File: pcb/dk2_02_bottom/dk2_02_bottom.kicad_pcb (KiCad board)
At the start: 2 copper layers, 140 x 108 mm, 174 parts, among them J1 Micro_SD_Card, J10 Trigger_Out_1, J11 Trigger_Out_4, J12 Trigger_Out_3, J13 Sync_Out, J14 Eurorack_Power, J2 CV_In_1, J3 CV_In_2, J4 CV_In_3, J5 CV_In_4, J6 Euro_Out_1, J7 Euro_Out_2, J8 Sync_Input, J9 Trigger_Out_2, Q1 MMBT3904, SW1 SW_Push, SW10 SW_Push, SW11 SW_Push, SW12 SW_Push, SW13 SW_Push, SW14 SW_Push, SW15 SW_Push, SW16 SW_Push, SW17 SW_Push, SW18 SW_Push, SW2 SW_Push, SW3 SW_Push, SW4 SW_Push, SW5 SW_Push, SW6 SW_Push, SW7 SW_Push, SW8 SW_Push, SW9 SW_Push, U1 Pico, U10 74HC4051, U11 AP7333-33SRG, U12 TL072, U13 PCM5102, U14 TL072, U15 TL072, U16 TL072, U17 XL1509-5.0, U2 74HC595, U3 74HC595, U4 CA56-12EWA, U5 74HC165, U6 74HC165, U7 74HC4051, U8 MCP6002-xSN, U9 MCP6002-xSN

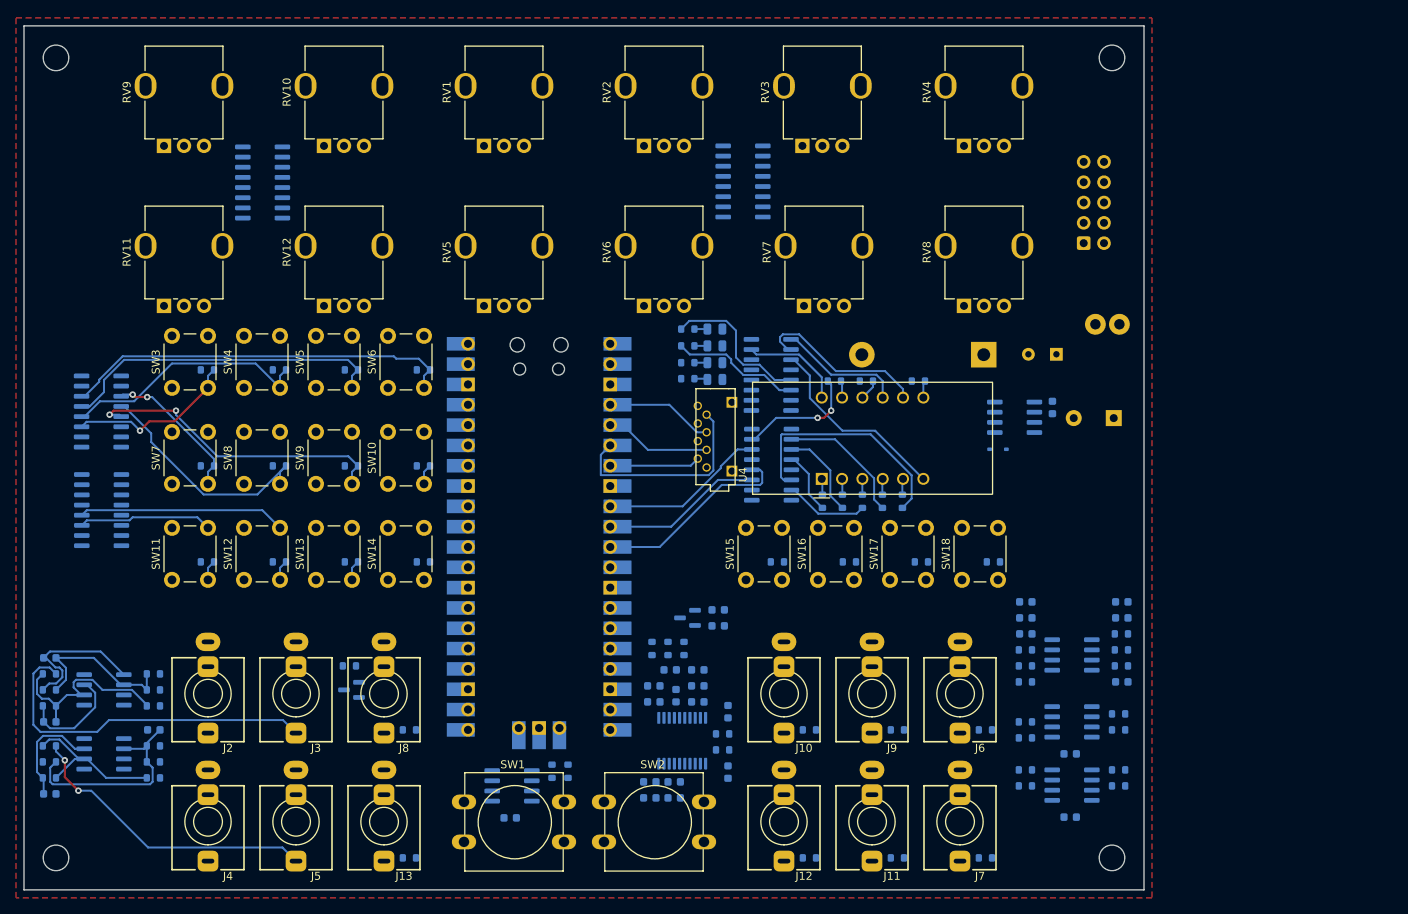
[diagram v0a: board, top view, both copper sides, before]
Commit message: bottom pcb looks fairly easy
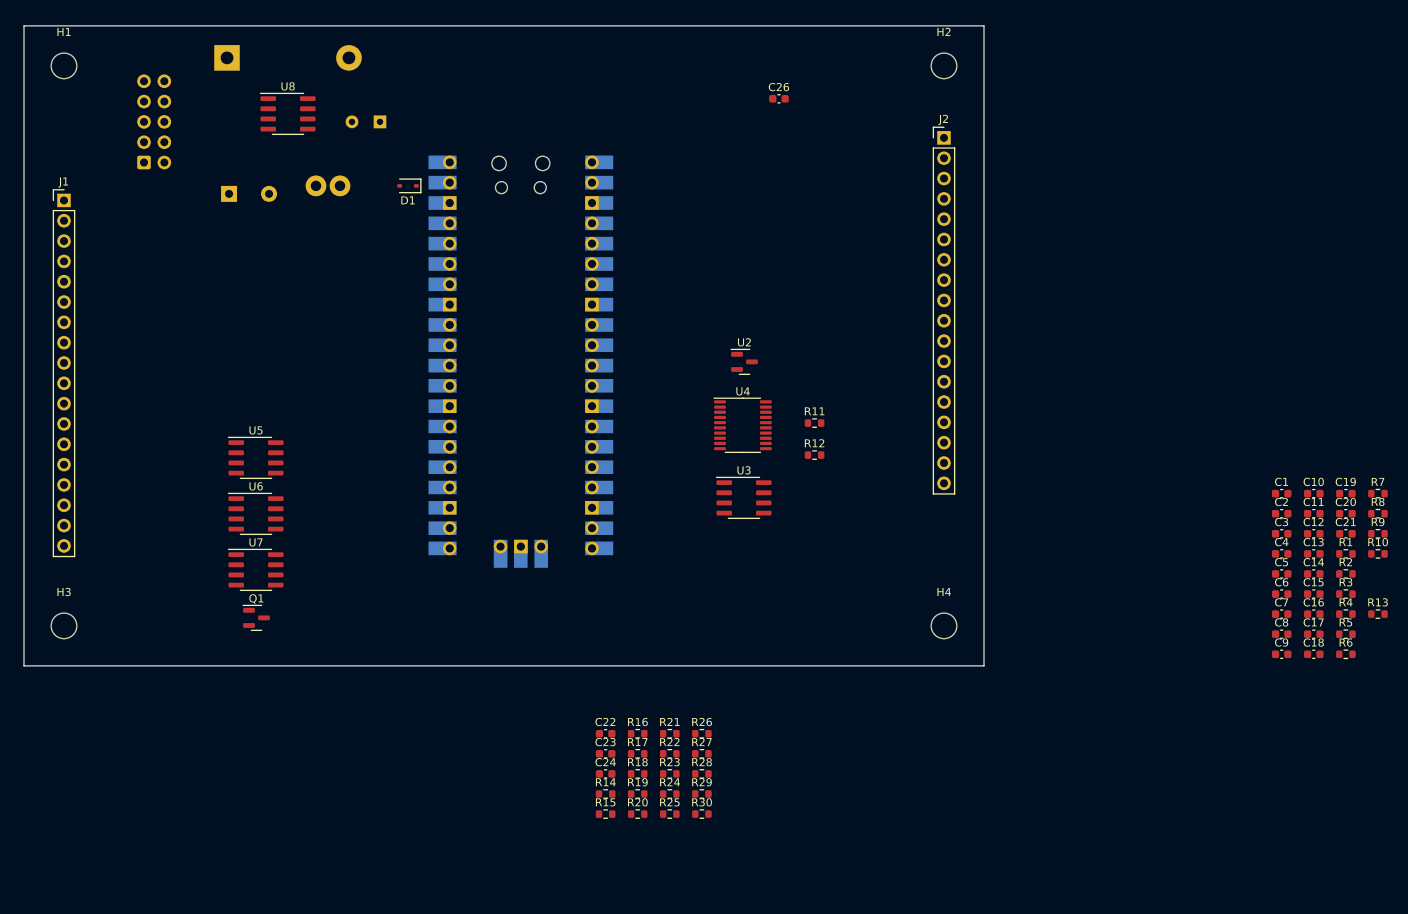
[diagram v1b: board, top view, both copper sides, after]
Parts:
- removed C28: 100n, Capacitor_SMD:C_0603_1608Metric
- removed C29: 470uF 35V, Capacitor_THT:CP_Radial_D10.0mm_P5.00mm
- removed C30: 1uF, Capacitor_SMD:C_0603_1608Metric
- removed C31: 180uF 35V, Capacitor_THT:CP_Radial_D8.0mm_P3.50mm
- removed D3, D4, D5: LED, LED_SMD:LED_0805_2012Metric
- removed D6: 1N5820, Diode_THT:D_DO-201AD_P15.24mm_Horizontal
- removed J10: Trigger_Out_1, AudioJacks:Jack_3.5mm_QingPu_WQP-PJ398SM_Vertical
- removed J11: Trigger_Out_4, AudioJacks:Jack_3.5mm_QingPu_WQP-PJ398SM_Vertical
- removed J12: Trigger_Out_3, AudioJacks:Jack_3.5mm_QingPu_WQP-PJ398SM_Vertical
- removed J13: Sync_Out, AudioJacks:Jack_3.5mm_QingPu_WQP-PJ398SM_Vertical
- removed J14: Eurorack_Power, Connector_IDC:IDC-Header_2x05_P2.54mm_Vertical
- removed J4: CV_In_3, AudioJacks:Jack_3.5mm_QingPu_WQP-PJ398SM_Vertical
- removed J5: CV_In_4, AudioJacks:Jack_3.5mm_QingPu_WQP-PJ398SM_Vertical
- removed J6: Euro_Out_1, AudioJacks:Jack_3.5mm_QingPu_WQP-PJ398SM_Vertical
- removed J7: Euro_Out_2, AudioJacks:Jack_3.5mm_QingPu_WQP-PJ398SM_Vertical
- removed J8: Sync_Input, AudioJacks:Jack_3.5mm_QingPu_WQP-PJ398SM_Vertical
- removed J9: Trigger_Out_2, AudioJacks:Jack_3.5mm_QingPu_WQP-PJ398SM_Vertical
- removed R31, R35, R37: 240k, Resistor_SMD:R_0603_1608Metric
- removed R32, R36, R38, R56, R57, R58, R59, R62, R63, R64, R65, R68, R69: 100k, Resistor_SMD:R_0603_1608Metric
- removed R33, R34, R39, R40: 33k, Resistor_SMD:R_0603_1608Metric
- removed R41, R42, R45, R46: 39k, Resistor_SMD:R_0603_1608Metric
- removed R43, R44: 5.6k, Resistor_SMD:R_0603_1608Metric
- removed R47, R48, R60, R61, R66, R67, R70: 1k, Resistor_SMD:R_0603_1608Metric
- removed R49, R50, R51: 56R, Resistor_SMD:R_0603_1608Metric
- removed R52, R53: 470R, Resistor_SMD:R_0603_1608Metric
- removed R54: 100K, Resistor_SMD:R_0603_1608Metric
- removed R55: 10K, Resistor_SMD:R_0603_1608Metric
- removed RV1, RV10, RV11, RV12, RV2, RV3, RV4, RV5, RV6, RV7, RV8, RV9: 10k, Library:Potentiometer_Alps_RK09K_vertical_biggerholes
- removed SW1, SW2: SW_Push, Button_Switch_THT:SW_PUSH-12mm
- removed SW10, SW11, SW12, SW13, SW14, SW15, SW16, SW17, SW18, SW3, SW4, SW5, SW6, SW7, SW8, SW9: SW_Push, Button_Switch_THT:SW_PUSH_6mm
- removed U10: 74HC4051, Package_SO:SOIC-16_3.9x9.9mm_P1.27mm
- removed U11: AP7333-33SRG, Package_TO_SOT_SMD:SOT-23
- removed U12, U14, U15, U16: TL072, Package_SO:SOIC-8_3.9x4.9mm_P1.27mm
- removed U13: PCM5102, Package_SO:TSSOP-20_4.4x6.5mm_P0.65mm
- removed U17: XL1509-5.0, Package_SO:SOIC-8_3.9x4.9mm_P1.27mm
- removed U9: MCP6002-xSN, Package_SO:SOIC-8_3.9x4.9mm_P1.27mm
- C1, C4: value 1n -> 1uF; moved to F.Cu
- C10, C26: value 100n -> 1uF; moved to F.Cu
- C11: value 18p -> 10uF; moved to F.Cu
- C12: value 18p -> 2.2uF; moved to F.Cu
- C13: value 0.1uF -> 2.2uF; moved to F.Cu
- C14: value 1uF -> 0.1uF; moved to F.Cu
- C15: value 10uF -> 1uF; moved to F.Cu
- C16: value 2.2uF -> 10uF; moved to F.Cu
- C17: value 2.2uF -> 0.1uF; moved to F.Cu
- C18, C20, D1, Q1: moved to F.Cu
- C19: value 1uF -> 2.2nF; moved to F.Cu
- C2, C3: value 1n -> 10uF; moved to F.Cu
- C21: value 0.1uF -> 2.2nF; moved to F.Cu
- C22: value 0.1uF -> 100n; moved to F.Cu
- C23: value 2.2nF -> 100n; moved to F.Cu
- C24, C6: value 10uF -> 100n; moved to F.Cu
- C25: value 2.2nF -> 470uF 35V; footprint Capacitor_SMD:C_0603_1608Metric -> Capacitor_THT:CP_Radial_D10.0mm_P5.00mm
- C27: value 100n -> 180uF 35V; footprint Capacitor_SMD:C_0603_1608Metric -> Capacitor_THT:CP_Radial_D8.0mm_P3.50mm
- C5: value 1uF -> 100n; moved to F.Cu
- C7: value 10uF -> 18p; moved to F.Cu
- C8: value 1uF -> 18p; moved to F.Cu
- C9: value 100n -> 0.1uF; moved to F.Cu
- D2: value LED -> 1N5820; footprint LED_SMD:LED_0805_2012Metric -> Diode_THT:D_DO-201AD_P15.24mm_Horizontal
- J1: value Micro_SD_Card -> Conn_01x18_Pin; footprint misc:YAMAICHI_MICROSD_VERTICAL -> Connector_PinHeader_2.54mm:PinHeader_1x18_P2.54mm_Vertical
- J2: value CV_In_1 -> Conn_01x18_Pin; footprint AudioJacks:Jack_3.5mm_QingPu_WQP-PJ398SM_Vertical -> Connector_PinHeader_2.54mm:PinHeader_1x18_P2.54mm_Vertical
- J3: value CV_In_2 -> Eurorack_Power; footprint AudioJacks:Jack_3.5mm_QingPu_WQP-PJ398SM_Vertical -> Connector_IDC:IDC-Header_2x05_P2.54mm_Vertical; moved to B.Cu
- R1, R2, R5, R6: value 200R -> 39k; moved to F.Cu
- R10, R11, R9: value 200R -> 56R; moved to F.Cu
- R12: value 200R -> 470R; moved to F.Cu
- R13: value 10k -> 470R; moved to F.Cu
- R14: value 10k -> 100K; moved to F.Cu
- R15: value 10k -> 10K; moved to F.Cu
- R16, R17, R18, R19, R22, R23, R24, R25, R28: value 10k -> 100k; moved to F.Cu
- R20, R21, R26, R27: value 10k -> 1k; moved to F.Cu
- R29: value 240k -> 100k; moved to F.Cu
- R3, R4: value 200R -> 5.6k; moved to F.Cu
- R30: value 100k -> 1k; moved to F.Cu
- R7, R8: value 200R -> 1k; moved to F.Cu
- U2: value 74HC595 -> AP7333-33SRG; footprint Package_SO:SOIC-16_3.9x9.9mm_P1.27mm -> Package_TO_SOT_SMD:SOT-23; moved to F.Cu
- U3: value 74HC595 -> TL072; footprint Package_SO:SOIC-16_3.9x9.9mm_P1.27mm -> Package_SO:SOIC-8_3.9x4.9mm_P1.27mm; moved to F.Cu
- U4: value CA56-12EWA -> PCM5102; footprint Library:SR410361N -> Package_SO:TSSOP-20_4.4x6.5mm_P0.65mm
- U5, U6: value 74HC165 -> TL072; footprint Package_SO:SOIC-16_3.9x9.9mm_P1.27mm -> Package_SO:SOIC-8_3.9x4.9mm_P1.27mm; moved to F.Cu
- U7: value 74HC4051 -> TL072; footprint Package_SO:SOIC-16_3.9x9.9mm_P1.27mm -> Package_SO:SOIC-8_3.9x4.9mm_P1.27mm; moved to F.Cu
- U8: value MCP6002-xSN -> XL1509-5.0; moved to F.Cu
- moved C4 156.9 mm to (237.2, 116.0), turned to 0 degrees
- moved C2 156.2 mm to (237.2, 111.0), turned to 0 degrees
- moved C1 155.4 mm to (237.2, 108.5), turned to 0 degrees
- moved R13 149.5 mm to (249.2, 123.5), turned to 0 degrees
- moved C3 143.1 mm to (237.2, 113.5), turned to 0 degrees
- moved C27 117.0 mm to (124.5, 62.0), turned to 180 degrees
- moved J2 115.3 mm to (195.0, 64.0), turned to 0 degrees
- moved L1 101.9 mm to (116.5, 70.0), turned to 0 degrees
- moved C26 96.9 mm to (174.4, 59.1)
- moved C25 95.5 mm to (105.6, 71.0), turned to 0 degrees
- moved C20 94.0 mm to (245.2, 111.0), turned to 0 degrees
- moved C19 91.4 mm to (245.2, 108.5)
- moved C21 90.2 mm to (245.2, 113.5)
- moved R4 88.1 mm to (245.2, 123.5), turned to 0 degrees
- moved R3 87.9 mm to (245.2, 121.0), turned to 0 degrees
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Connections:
- C1 pad 1: Net-(U8A--) -> +5V
- C1 pad 2: CV_IN_1 -> GND
- C10 pad 1: GND -> +3.3VDAC
- C10 pad 2: -12V -> GND
- C11 pad 1: Net-(U12A--) -> +3.3VDAC
- C11 pad 2: Net-(C11-Pad2) -> GND
- C12 pad 1: Net-(U12B--) -> Net-(U4-CAPP)
- C12 pad 2: Net-(C12-Pad2) -> Net-(U4-CAPM)
- C13 pad 1: +3.3VDAC -> Net-(U4-VNEG)
- C15 pad 1: +3.3VDAC -> Net-(U4-LDOO)
- C16 pad 1: Net-(U13-CAPP) -> +3.3VDAC
- C16 pad 2: Net-(U13-CAPM) -> GND
- C17 pad 1: Net-(U13-VNEG) -> Net-(U4-LDOO)
- C19 pad 1: Net-(U13-LDOO) -> LINE_OUT_L
- C2 pad 1: Net-(U8B--) -> LINE_OUT_L
- C2 pad 2: CV_IN_2 -> Net-(C2-Pad2)
- C21 pad 1: Net-(U13-LDOO) -> LINE_OUT_R
- C22 pad 1: +3.3VDAC -> +12V
- C22 pad 2: GND -> -12V
- C23 pad 1: LINE_OUT_L -> +12V
- C23 pad 2: GND -> -12V
- C24 pad 1: +3.3VDAC -> +12V
- C24 pad 2: GND -> -12V
- C25 pad 1: LINE_OUT_R -> +12V
- C26 pad 2: -12V -> GND
- C27 pad 1: +12V -> +5V
- C27 pad 2: -12V -> GND
- C3 pad 1: Net-(U9A--) -> LINE_OUT_R
- C3 pad 2: CV_IN_3 -> Net-(C3-Pad2)
- C4 pad 1: Net-(U9B--) -> +3.3VDAC
- C4 pad 2: CV_IN_4 -> GND
- C5 pad 1: +5V -> +12V
- C6 pad 1: LINE_OUT_L -> GND
- C6 pad 2: Net-(C6-Pad2) -> -12V
- C7 pad 1: LINE_OUT_R -> Net-(U3A--)
- C8 pad 1: +3.3VDAC -> Net-(U3B--)
- C8 pad 2: GND -> Net-(C8-Pad2)
- C9 pad 1: +12V -> +3.3VDAC
- D2 pad 1: GND -> Net-(D2-K)
- D2 pad 2: Net-(D2-A) -> GND
- J1 pad 2: SD_CHIP_SELECT -> unconnected-(J1-Pin_2-Pad2)
- J1 pad 3: SD_SERIAL_IN -> unconnected-(J1-Pin_3-Pad3)
- J1 pad 4: +3.3V -> START_STOP_BUTTON
- J1 pad 5: SD_CLOCK -> TAP_TEMPO_BUTTON
- J1 pad 6: GND -> 165_LOAD
- J1 pad 7: SD_SERIAL_OUT -> 165_CLOCK
- J1 pad 8: unconnected-(J1-DAT1-Pad8) -> 165_DATA
- J1 pad 9: GND -> TRIGGER_OUT_1_EURO
- L1 pad 1: Net-(D6-K) -> Net-(D2-K)
- R1 pad 1: Net-(D2-A) -> Net-(C2-Pad2)
- R1 pad 2: Net-(U3-QE) -> GND
- R10 pad 1: Net-(U4-f) -> DAC_DOUT
- R10 pad 2: Net-(U2-QF) -> Net-(U4-DIN)
- R11 pad 1: Net-(U4-g) -> DAC_LRC
- R11 pad 2: Net-(U2-QG) -> Net-(U4-LRCK)
- R12 pad 1: Net-(U4-DPX) -> Net-(U4-OUTL)
- R12 pad 2: Net-(U2-QH) -> LINE_OUT_L
- R13 pad 1: Net-(U5-D0) -> Net-(U4-OUTR)
- R13 pad 2: GND -> LINE_OUT_R
- R14 pad 1: Net-(U5-D1) -> SYNC_IN_EURO
- R14 pad 2: GND -> Net-(Q1-B)
- R15 pad 1: Net-(U5-D2) -> +3.3V
- R15 pad 2: GND -> SYNC_IN
- R16 pad 1: Net-(U5-D3) -> Net-(U5B--)
- R17 pad 1: Net-(U5-D4) -> Net-(U5A--)
- R18 pad 1: Net-(U5-D5) -> Net-(R18-Pad1)
- R18 pad 2: GND -> Net-(U5B--)
- R19 pad 1: Net-(U5-D6) -> Net-(R19-Pad1)
- R19 pad 2: GND -> Net-(U5A--)
- R2 pad 1: Net-(D3-A) -> Net-(C3-Pad2)
- R2 pad 2: Net-(U3-QF) -> GND
- R20 pad 1: Net-(U5-D7) -> Net-(R18-Pad1)
- R20 pad 2: GND -> TRIGGER_OUT_2_EURO
- R21 pad 1: Net-(U6-D0) -> Net-(R19-Pad1)
- R21 pad 2: GND -> TRIGGER_OUT_1_EURO
- R22 pad 1: Net-(U6-D1) -> Net-(U6B--)
- R23 pad 1: Net-(U6-D2) -> Net-(U6A--)
- R24 pad 1: Net-(U6-D3) -> Net-(R24-Pad1)
- R24 pad 2: GND -> Net-(U6B--)
- R25 pad 1: Net-(U6-D4) -> Net-(R25-Pad1)
- R25 pad 2: GND -> Net-(U6A--)
- R26 pad 1: Net-(U6-D5) -> Net-(R24-Pad1)
- R26 pad 2: GND -> TRIGGER_OUT_4_EURO
- R27 pad 1: Net-(U6-D6) -> Net-(R25-Pad1)
- R27 pad 2: GND -> TRIGGER_OUT_3_EURO
- R28 pad 1: Net-(U6-D7) -> Net-(U7A--)
- R29 pad 1: -12V -> Net-(R29-Pad1)
- R29 pad 2: Net-(U8A--) -> Net-(U7A--)
- R3 pad 1: Net-(D4-A) -> Net-(C2-Pad2)
- R3 pad 2: Net-(U3-QG) -> Net-(U3A--)
- R30 pad 1: Net-(J2-PadT) -> Net-(R29-Pad1)
- R30 pad 2: Net-(U8A--) -> SYNC_OUT_EURO
- R4 pad 1: Net-(D5-A) -> Net-(C3-Pad2)
- R4 pad 2: Net-(U3-QH) -> Net-(U3B--)
- R5 pad 1: Net-(U4-a) -> Net-(U3A--)
- R5 pad 2: Net-(U2-QA) -> Net-(C7-Pad2)
- R6 pad 1: Net-(U4-b) -> Net-(U3B--)
- R6 pad 2: Net-(U2-QB) -> Net-(C8-Pad2)
- R7 pad 1: Net-(U4-c) -> Net-(C7-Pad2)
- R7 pad 2: Net-(U2-QC) -> EURO_OUT_1
- R8 pad 1: Net-(U4-d) -> Net-(C8-Pad2)
- R8 pad 2: Net-(U2-QD) -> EURO_OUT_2
- R9 pad 1: Net-(U4-e) -> DAC_BCLK
- R9 pad 2: Net-(U2-QE) -> Net-(U4-BCK)
- U2 pad 1: Net-(U2-QB) -> +5V
- U2 pad 2: Net-(U2-QC) -> +3.3VDAC
- U2 pad 3: Net-(U2-QD) -> GND
- U3 pad 1: Net-(U3-QB) -> Net-(C7-Pad2)
- U3 pad 2: Net-(U3-QC) -> Net-(U3A--)
- U3 pad 3: Net-(U3-QD) -> GND
- U3 pad 4: Net-(U3-QE) -> -12V
- U3 pad 5: Net-(U3-QF) -> GND
- U3 pad 6: Net-(U3-QG) -> Net-(U3B--)
- U3 pad 7: Net-(U3-QH) -> Net-(C8-Pad2)
- U3 pad 8: GND -> +12V
- U4 pad 1: Net-(U4-e) -> +3.3VDAC
- U4 pad 10: Net-(U4-f) -> GND
- U4 pad 11: Net-(U4-a) -> GND
- U4 pad 12: Net-(U3-QA) -> GND
- U4 pad 2: Net-(U4-d) -> Net-(U4-CAPP)
- U4 pad 3: Net-(U4-DPX) -> GND
- U4 pad 4: Net-(U4-c) -> Net-(U4-CAPM)
- U4 pad 5: Net-(U4-g) -> Net-(U4-VNEG)
- U4 pad 6: Net-(U3-QD) -> Net-(U4-OUTL)
- U4 pad 7: Net-(U4-b) -> Net-(U4-OUTR)
- U4 pad 8: Net-(U3-QC) -> +3.3VDAC
- U4 pad 9: Net-(U3-QB) -> GND
- U5 pad 1: 165_LOAD -> Net-(R19-Pad1)
- U5 pad 2: 165_CLOCK -> Net-(U5A--)
- U5 pad 3: Net-(U5-D4) -> TRIGGER_OUT_1
- U5 pad 4: Net-(U5-D5) -> -12V
- U5 pad 5: Net-(U5-D6) -> TRIGGER_OUT_2
- U5 pad 6: Net-(U5-D7) -> Net-(U5B--)
- U5 pad 7: unconnected-(U5-~{Q7}-Pad7) -> Net-(R18-Pad1)
- U5 pad 8: GND -> +12V
- U6 pad 1: 165_LOAD -> Net-(R25-Pad1)
- U6 pad 2: 165_CLOCK -> Net-(U6A--)
- U6 pad 3: Net-(U6-D4) -> TRIGGER_OUT_3
- U6 pad 4: Net-(U6-D5) -> -12V
- U6 pad 5: Net-(U6-D6) -> TRIGGER_OUT_4
- U6 pad 6: Net-(U6-D7) -> Net-(U6B--)
- U6 pad 7: unconnected-(U6-~{Q7}-Pad7) -> Net-(R24-Pad1)
- U6 pad 8: GND -> +12V
- U7 pad 1: Net-(U7-A4) -> Net-(R29-Pad1)
- U7 pad 2: Net-(U7-A6) -> Net-(U7A--)
- U7 pad 3: 4051_READING_0 -> SYNC_OUT
- U7 pad 4: Net-(U7-A7) -> -12V
- U7 pad 5: Net-(U7-A5) -> GND
- U7 pad 6: GND -> Net-(U7B--)
- U7 pad 7: GND -> Net-(U7B--)
- U7 pad 8: GND -> +12V
- U8 pad 1: CV_IN_1 -> +12V
- U8 pad 2: Net-(U8A--) -> Net-(D2-K)
- U8 pad 3: GND -> +5V
- U8 pad 6: Net-(U8B--) -> GND
- U8 pad 7: CV_IN_2 -> GND
- U8 pad 8: +3.3V -> GND
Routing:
- net Net-(U5-D3): track 49.0 -> 0.00 mm
- net Net-(J3-PadT): track 44.4 -> 0.00 mm
- net Net-(U5-D2): track 40.9 -> 0.00 mm
- net Net-(U5-D6): track 38.5 -> 0.00 mm, vias 2 -> 0
- net Net-(J5-PadT): track 37.6 -> 0.00 mm, vias 2 -> 0
- net Net-(U5-D1): track 31.4 -> 0.00 mm
- net Net-(U5-D5): track 29.8 -> 0.00 mm
- net Net-(U2-QG): track 29.7 -> 0.00 mm
- net Net-(U6-D1): track 28.5 -> 0.00 mm
- net Net-(U9A--): track 26.3 -> 0.00 mm
- net SD_SERIAL_OUT: track 25.8 -> 0.00 mm
- net 595_LATCH: track 25.1 -> 0.00 mm
- net Net-(U8B--): track 24.9 -> 0.00 mm
- net Net-(U3-QD): track 24.4 -> 0.00 mm
- net Net-(U5-D0): track 22.1 -> 0.00 mm, vias 1 -> 0
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- removed copper zone on F.Cu, net GND
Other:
- board size 140 x 108 mm -> 120 x 80 mm
- board text removed: "REALISED THAT THIS SHOULD BE A DOUBLE-DECKER BOARD"

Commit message: started top side pcb
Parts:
- moved H1 1.41 mm to (84.0, 54.0)
- moved H2 1.41 mm to (196.0, 54.0)
- moved H3 1.41 mm to (84.0, 126.0)
- moved H4 1.41 mm to (196.0, 126.0)
- moved J2 1.00 mm to (194.9, 65.0)
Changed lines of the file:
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@@
   )
   (footprint "MountingHole:MountingHole_3.2mm_M3" (layer "F.Cu")
-    (at 195 125)
+    (at 196 126)
     (descr "Mounting Hole 3.2mm, no annular, M3")
     (tags "mounting hole 3.2mm no annular m3")
@@
   )
   (footprint "MountingHole:MountingHole_3.2mm_M3" (layer "F.Cu")
-    (at 85 125)
+    (at 84 126)
     (descr "Mounting Hole 3.2mm, no annular, M3")
     (tags "mounting hole 3.2mm no annular m3")
@@
   )
   (footprint "MountingHole:MountingHole_3.2mm_M3" (layer "F.Cu")
-    (at 195 55)
+    (at 196 54)
     (descr "Mounting Hole 3.2mm, no annular, M3")
     (tags "mounting hole 3.2mm no annular m3")
@@
   )
   (footprint "MountingHole:MountingHole_3.2mm_M3" (layer "F.Cu")
-    (at 85 55)
+    (at 84 54)
     (descr "Mounting Hole 3.2mm, no annular, M3")
     (tags "mounting hole 3.2mm no annular m3")
@@
   )
   (footprint "Connector_PinHeader_2.54mm:PinHeader_1x18_P2.54mm_Vertical" (layer "F.Cu")
-    (at 195 64)
+    (at 194.9 65)
     (descr "Through hole straight pin header, 1x18, 2.54mm pitch, single row")
     (tags "Through hole pin header THT 1x18 2.54mm single row")

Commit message: done for the week, started routing
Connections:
- J2 pad 10: SD_SERIAL_IN -> 595_DATA
- J2 pad 11: SD_SERIAL_OUT -> 595_CLOCK
- J2 pad 12: SD_CHIP_SELECT -> 595_LATCH
- J2 pad 6: 595_DATA -> SD_CLOCK
- J2 pad 7: 595_CLOCK -> SD_SERIAL_IN
- J2 pad 8: 595_LATCH -> SD_SERIAL_OUT
- J2 pad 9: SD_CLOCK -> SD_CHIP_SELECT
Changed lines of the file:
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@@
   (net 78 "TRIGGER_OUT_3")
   (net 79 "TRIGGER_OUT_2")
-  (net 80 "Net-(D1-K)")
+  (net 80 "Net-(#FLG02-pwr)")
   (footprint "Diode_SMD:D_SOD-323" (layer "F.Cu")
     (at 128 70 180)
@@
       (stroke (width 0.1) (type solid)) (layer "F.Fab"))
     (pad "1" smd roundrect (at -1.05 0 180) (size 0.6 0.45) (layers "F.Cu" "F.Paste" "F.Mask") (roundrect_rratio 0.25)
-      (net 80 "Net-(D1-K)") (pinfunction "K") (pintype "passive"))
+      (net 80 "Net-(#FLG02-pwr)") (pinfunction "K") (pintype "passive"))
     (pad "2" smd roundrect (at 1.05 0 180) (size 0.6 0.45) (layers "F.Cu" "F.Paste" "F.Mask") (roundrect_rratio 0.25)
       (net 41 "+5V") (pinfunction "A") (pintype "passive"))
@@
       (net 35 "4051_READING_0") (pinfunction "Pin_5") (pintype "passive"))
     (pad "6" thru_hole oval (at 0 12.7) (size 1.7 1.7) (drill 1) (layers "*.Cu" "*.Mask")
-      (net 21 "595_DATA") (pinfunction "Pin_6") (pintype "passive"))
+      (net 17 "SD_CLOCK") (pinfunction "Pin_6") (pintype "passive"))
     (pad "7" thru_hole oval (at 0 15.24) (size 1.7 1.7) (drill 1) (layers "*.Cu" "*.Mask")
-      (net 22 "595_CLOCK") (pinfunction "Pin_7") (pintype "passive"))
+      (net 19 "SD_SERIAL_IN") (pinfunction "Pin_7") (pintype "passive"))
     (pad "8" thru_hole oval (at 0 17.78) (size 1.7 1.7) (drill 1) (layers "*.Cu" "*.Mask")
-      (net 23 "595_LATCH") (pinfunction "Pin_8") (pintype "passive"))
+      (net 18 "SD_SERIAL_OUT") (pinfunction "Pin_8") (pintype "passive"))
     (pad "9" thru_hole oval (at 0 20.32) (size 1.7 1.7) (drill 1) (layers "*.Cu" "*.Mask")
-      (net 17 "SD_CLOCK") (pinfunction "Pin_9") (pintype "passive"))
+      (net 20 "SD_CHIP_SELECT") (pinfunction "Pin_9") (pintype "passive"))
     (pad "10" thru_hole oval (at 0 22.86) (size 1.7 1.7) (drill 1) (layers "*.Cu" "*.Mask")
-      (net 19 "SD_SERIAL_IN") (pinfunction "Pin_10") (pintype "passive"))
+      (net 21 "595_DATA") (pinfunction "Pin_10") (pintype "passive"))
     (pad "11" thru_hole oval (at 0 25.4) (size 1.7 1.7) (drill 1) (layers "*.Cu" "*.Mask")
-      (net 18 "SD_SERIAL_OUT") (pinfunction "Pin_11") (pintype "passive"))
+      (net 22 "595_CLOCK") (pinfunction "Pin_11") (pintype "passive"))
     (pad "12" thru_hole oval (at 0 27.94) (size 1.7 1.7) (drill 1) (layers "*.Cu" "*.Mask")
-      (net 20 "SD_CHIP_SELECT") (pinfunction "Pin_12") (pintype "passive"))
+      (net 23 "595_LATCH") (pinfunction "Pin_12") (pintype "passive"))
     (pad "13" thru_hole oval (at 0 30.48) (size 1.7 1.7) (drill 1) (layers "*.Cu" "*.Mask")
       (net 49 "EURO_OUT_1") (pinfunction "Pin_13") (pintype "passive"))
@@
       (net 4 "GND") (pinfunction "GND") (pintype "bidirectional"))
     (pad "39" thru_hole oval (at 8.89 21.59 180) (size 1.7 1.7) (drill 1.02) (layers "*.Cu" "*.Mask")
-      (net 80 "Net-(D1-K)") (pinfunction "VSYS") (pintype "power_in"))
+      (net 80 "Net-(#FLG02-pwr)") (pinfunction "VSYS") (pintype "power_in"))
     (pad "39" smd rect (at 8.89 21.59 180) (size 3.5 1.7) (drill (offset 0.9 0)) (layers "B.Cu" "B.Mask")
-      (net 80 "Net-(D1-K)") (pinfunction "VSYS") (pintype "power_in"))
+      (net 80 "Net-(#FLG02-pwr)") (pinfunction "VSYS") (pintype "power_in"))
     (pad "40" thru_hole oval (at 8.89 24.13 180) (size 1.7 1.7) (drill 1.02) (layers "*.Cu" "*.Mask")
       (net 73 "unconnected-(U1-VBUS-Pad40)") (pinfunction "VBUS") (pintype "power_in+no_connect"))

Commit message: top routing done
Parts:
- moved J2 11.9 mm to (196.0, 76.8)
- moved J1 4.12 mm to (84.0, 75.8)
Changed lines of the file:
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@@
   )
   (footprint "Connector_PinHeader_2.54mm:PinHeader_1x18_P2.54mm_Vertical" (layer "F.Cu")
-    (at 85 71.82)
+    (at 84 75.82)
     (descr "Through hole straight pin header, 1x18, 2.54mm pitch, single row")
     (tags "Through hole pin header THT 1x18 2.54mm single row")
@@
   )
   (footprint "Connector_PinHeader_2.54mm:PinHeader_1x18_P2.54mm_Vertical" (layer "F.Cu")
-    (at 194.9 65)
+    (at 196 76.82)
     (descr "Through hole straight pin header, 1x18, 2.54mm pitch, single row")
     (tags "Through hole pin header THT 1x18 2.54mm single row")
